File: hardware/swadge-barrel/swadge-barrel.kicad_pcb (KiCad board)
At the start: 2 copper layers, 70.4 x 89.6 mm, 48 parts, among them J1 USB_B_Micro, Q1 Q_NPN_BEC, SW1 SW_SPDT, U1 ESP-13-WROOM-02D, U2 OLED_DISPLAY, U3 BUS_PCIexpress, U4 QMA6981, U5 AP1117-33, U6 OLED_CONNECTOR

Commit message: Fixed 3D model paths, Updated to version 1.0.1
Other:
- board text added: "Barrel 1.0.1"
- board text removed: "Barrel 1.0.0"

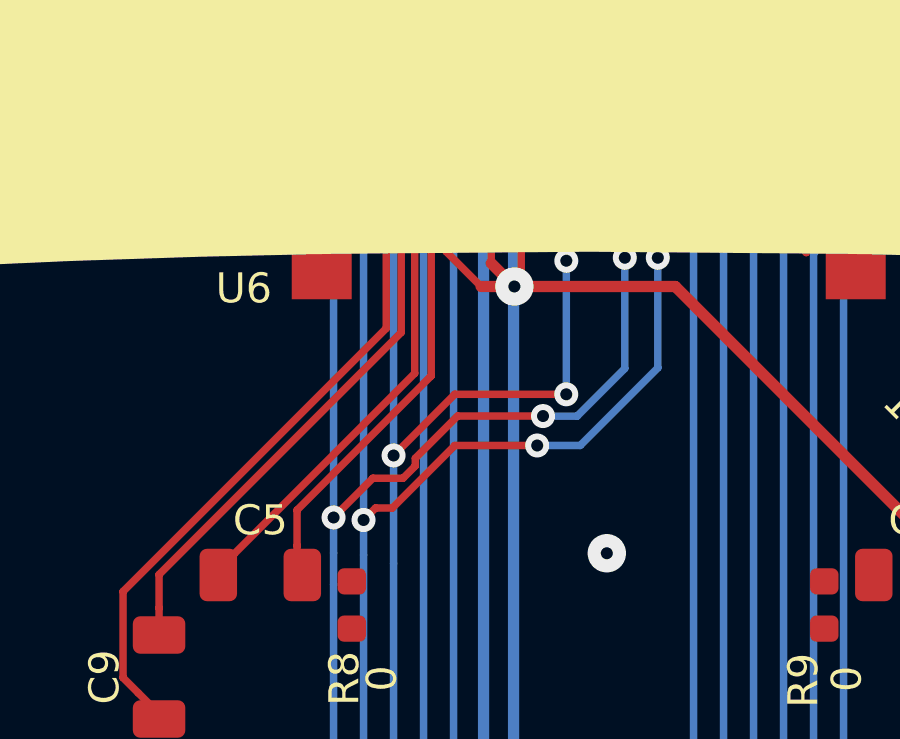
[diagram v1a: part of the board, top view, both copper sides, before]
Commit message: Fixed some bent traces
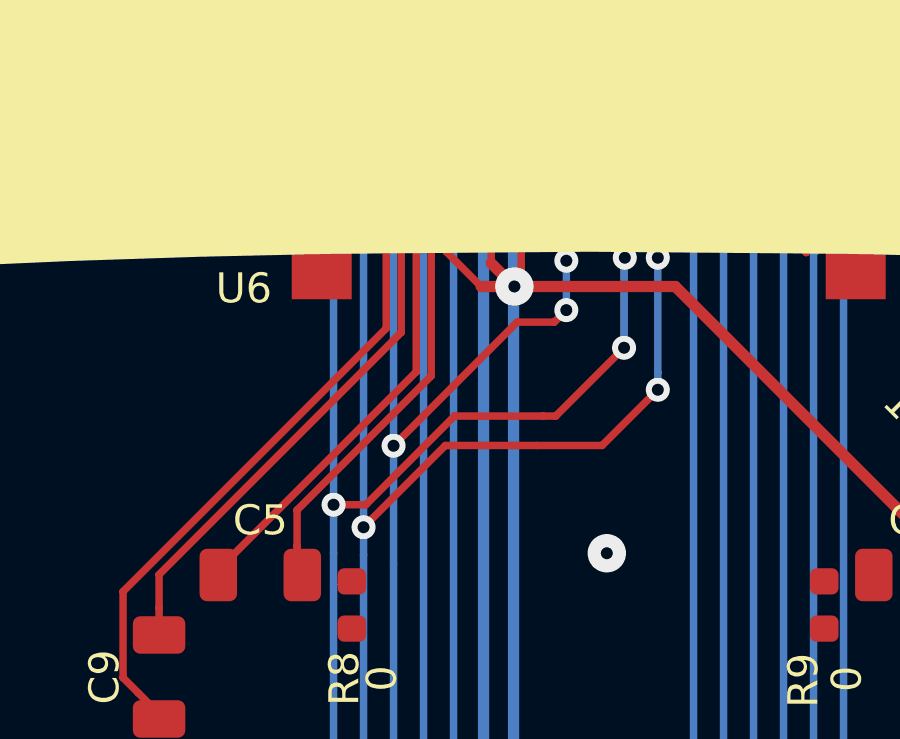
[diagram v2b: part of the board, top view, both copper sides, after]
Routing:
- net _RES: track 126.7 -> 124.9 mm
- net SCL: track 139.9 -> 139.2 mm
- net SDA: track 145.9 -> 146.4 mm

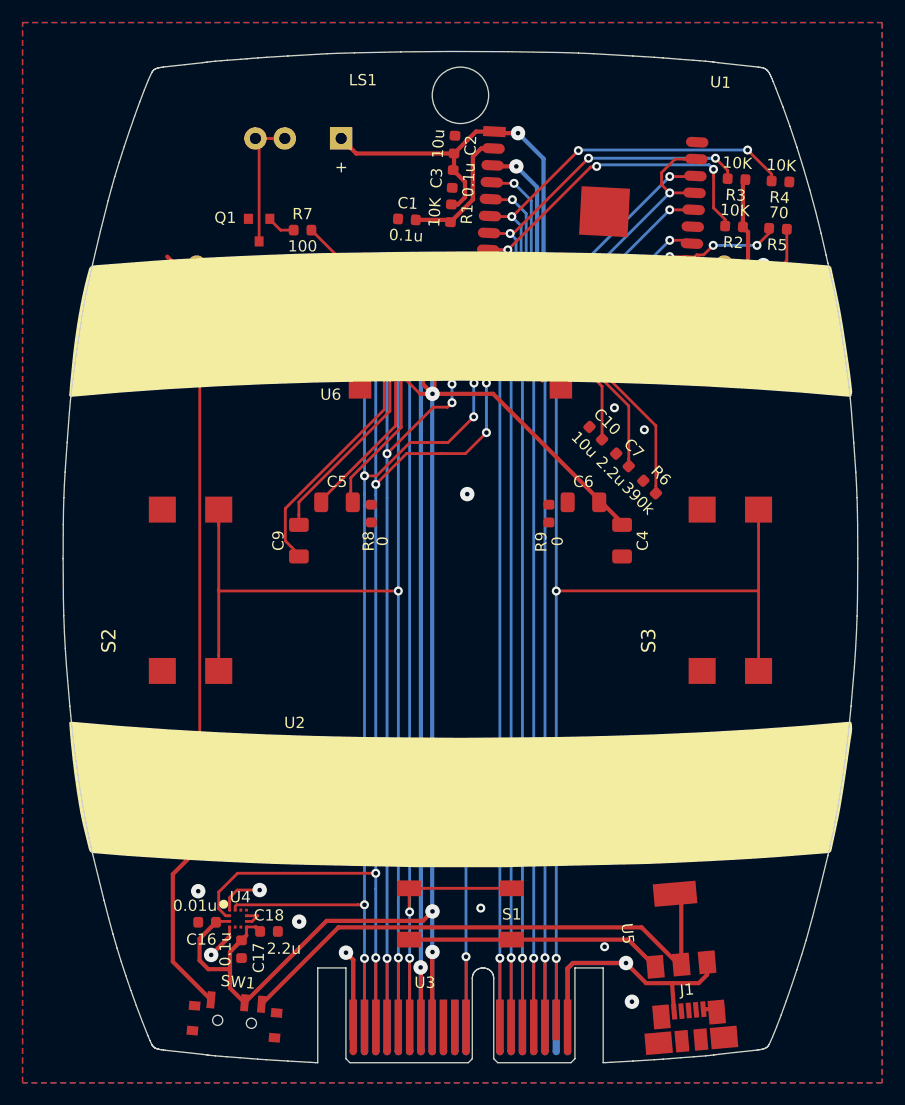
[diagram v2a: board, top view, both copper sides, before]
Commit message: #26 Remapped buttons to match devkit gpios
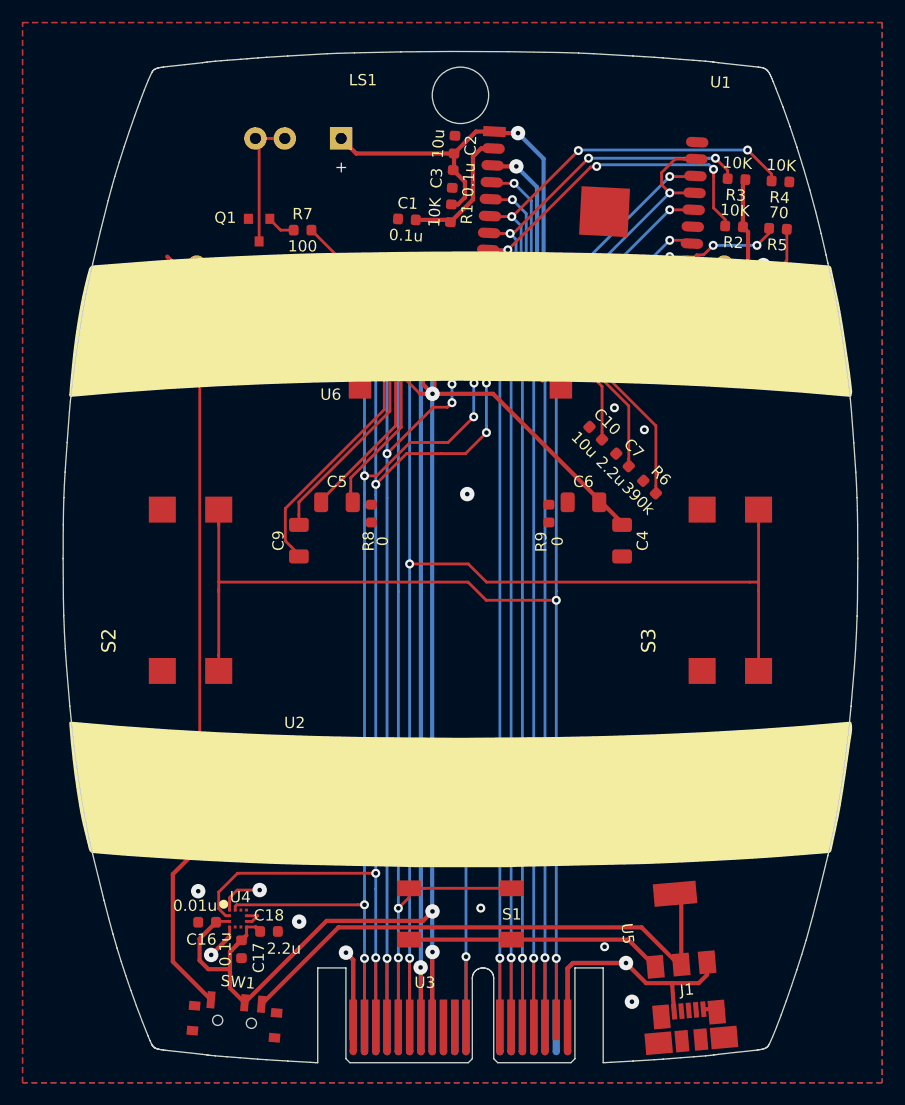
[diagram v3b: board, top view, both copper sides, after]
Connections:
- J1 pad 2: (no net) -> Net-(J1-Pad2)
- J1 pad 3: (no net) -> Net-(J1-Pad3)
- J1 pad 4: (no net) -> Net-(J1-Pad4)
- S1 pad 1: SW1 -> SW2
- S1 pad 2: SW1 -> SW2
- S2 pad 1: SW2 -> SW3
- S2 pad 2: SW2 -> SW3
- S3 pad 1: SW3 -> SW1
- S3 pad 2: SW3 -> SW1
- U4 pad 10: (no net) -> Net-(U4-Pad10)
- U4 pad 11: (no net) -> Net-(U4-Pad11)
- U4 pad 5: (no net) -> Net-(U4-Pad5)
- U4 pad 6: (no net) -> Net-(U4-Pad6)
- U6 pad 7: (no net) -> Net-(U6-Pad7)
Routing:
- net SW1: track 100.1 -> 134.7 mm
- net SW2: track 119.1 -> 98.7 mm
- net SW3: track 110.5 -> 124.7 mm

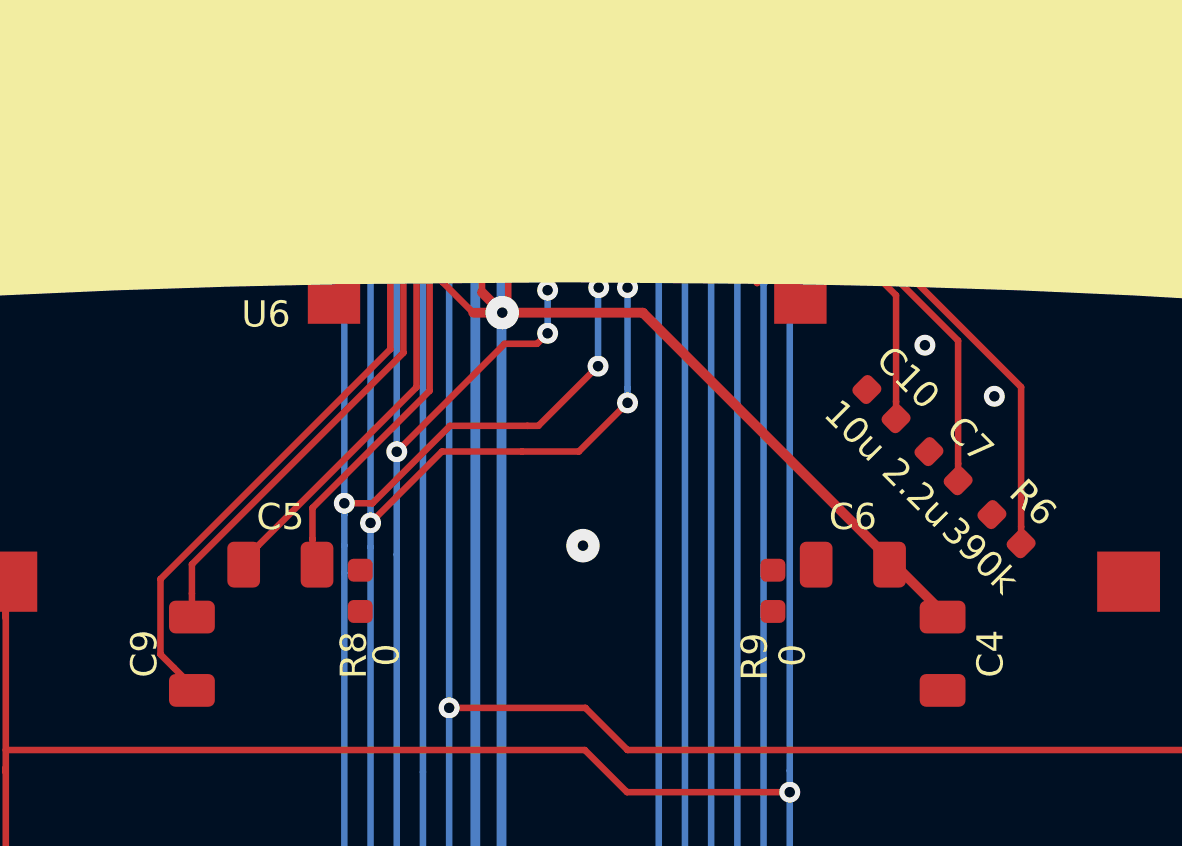
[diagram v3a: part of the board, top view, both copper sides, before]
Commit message: Flipped OLED contacts, haven't routed them yet #24
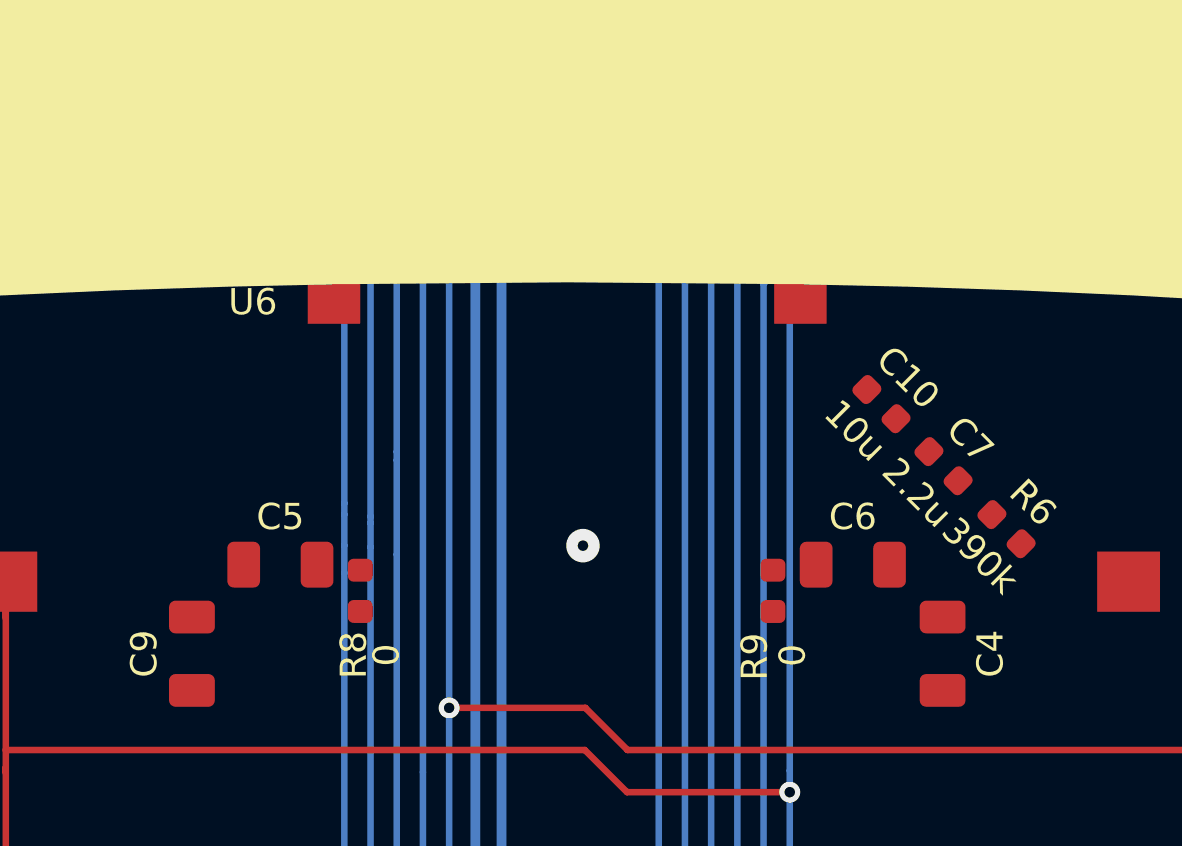
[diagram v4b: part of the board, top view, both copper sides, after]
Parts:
- U6: footprint Swadge_Parts:oled-flat_copy -> Swadge_Parts:ER-OLED0.96-1.3
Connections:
- U6 pad 31: (no net) -> GND
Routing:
- net GND: track 90.1 -> 54.7 mm, vias 13 -> 11
- net +3V3: track 305.2 -> 271.3 mm, vias 6 -> 5
- net Net-(R6-Pad2): track 23.3 -> 0.00 mm
- net Net-(C9-Pad1): track 21.8 -> 0.00 mm
- net SDA: track 146.4 -> 125.1 mm, vias 8 -> 5
- net Net-(C7-Pad2): track 18.6 -> 0.00 mm
- net Net-(C9-Pad2): track 18.2 -> 0.00 mm
- net SCL: track 139.2 -> 121.8 mm, vias 8 -> 5
- net Net-(C5-Pad1): track 15.8 -> 0.00 mm
- net Net-(C5-Pad2): track 14.9 -> 0.00 mm
- net Net-(C10-Pad2): track 13.9 -> 0.00 mm
- net _RES: track 124.9 -> 113.0 mm, vias 7 -> 4

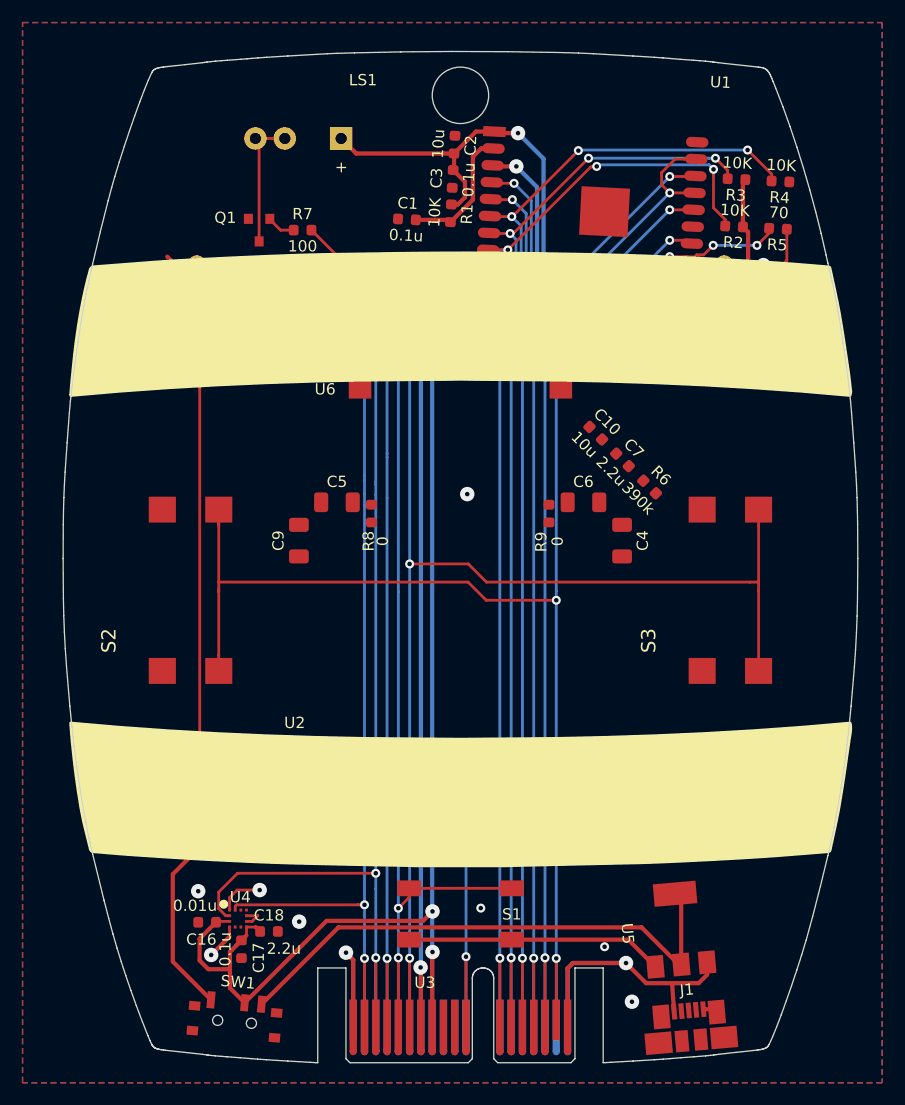
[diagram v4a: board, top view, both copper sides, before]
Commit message: #24 Rerouted OLED traces
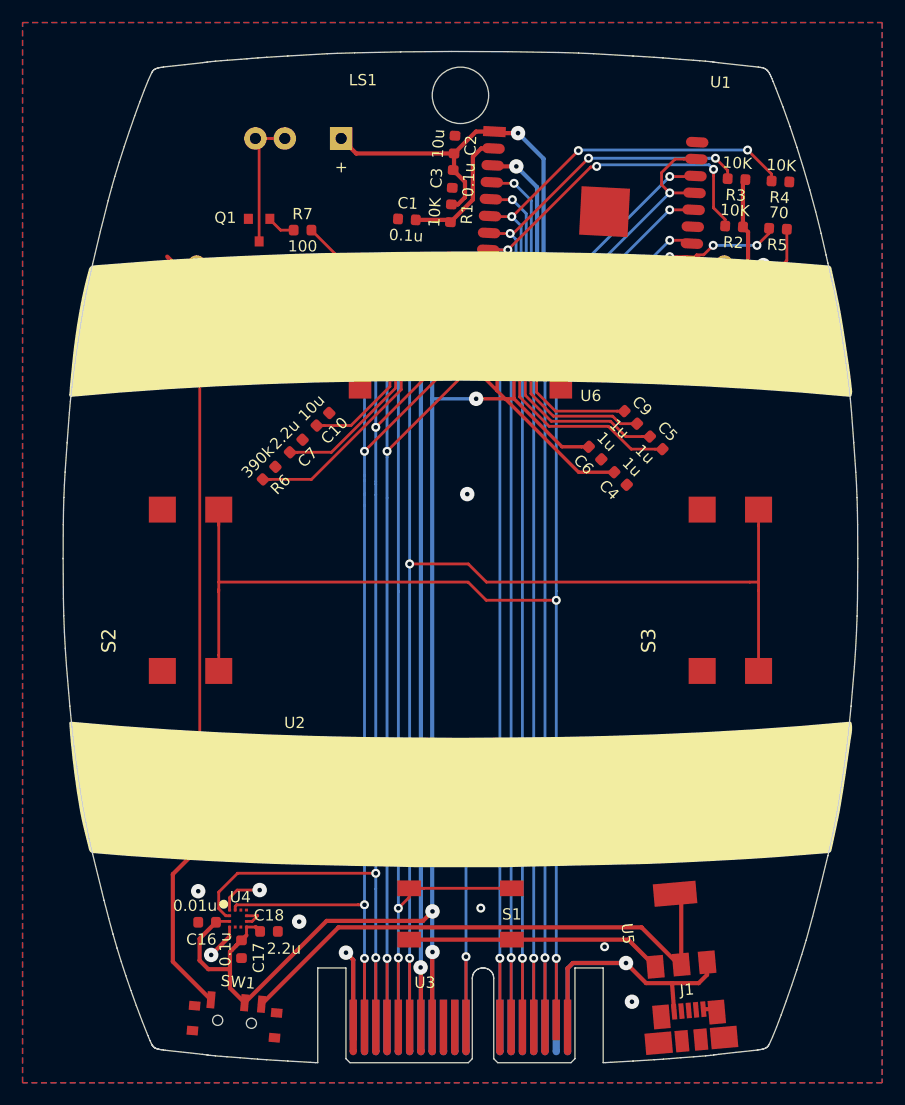
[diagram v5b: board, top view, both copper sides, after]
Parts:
- removed R8, R9: 0, Swadge_Parts:R_0603_1608Metric
- C4, C5, C6, C9: footprint Swadge_Parts:C_1206_3216Metric -> Swadge_Parts:C_0603_1608Metric
- moved R6 33.7 mm to (128.5, 90.7), turned to 225 degrees
- moved C9 31.4 mm to (160.6, 85.8), turned to 315 degrees
- moved C7 28.9 mm to (130.9, 88.3), turned to 225 degrees
- moved C5 28.8 mm to (162.8, 88.1), turned to 315 degrees
- moved C10 24.2 mm to (133.3, 86.0), turned to 225 degrees
- moved C4 5.51 mm to (159.7, 91.2), turned to 135 degrees
- moved C6 4.48 mm to (157.4, 89.0), turned to 135 degrees
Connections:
- J1 pad 2: Net-(J1-Pad2) -> (no net)
- J1 pad 3: Net-(J1-Pad3) -> (no net)
- J1 pad 4: Net-(J1-Pad4) -> (no net)
- U4 pad 10: Net-(U4-Pad10) -> (no net)
- U4 pad 11: Net-(U4-Pad11) -> (no net)
- U4 pad 5: Net-(U4-Pad5) -> (no net)
- U4 pad 6: Net-(U4-Pad6) -> (no net)
- U6 pad 7: Net-(U6-Pad7) -> (no net)
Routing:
- net +3V3: track 271.3 -> 310.9 mm, vias 5 -> 6
- net GND: track 54.7 -> 88.8 mm
- net Net-(R6-Pad2): track 0.00 -> 18.6 mm
- net Net-(C5-Pad2): track 0.00 -> 18.3 mm
- net Net-(C5-Pad1): track 0.00 -> 16.1 mm
- net Net-(C7-Pad2): track 0.00 -> 14.6 mm
- net Net-(C9-Pad2): track 0.00 -> 13.9 mm
- net Net-(C9-Pad1): track 0.00 -> 11.8 mm
- net _RES: track 113.0 -> 124.6 mm, vias 4 -> 5
- net SCL: track 121.8 -> 133.3 mm, vias 5 -> 6
- net Net-(C10-Pad2): track 0.00 -> 10.7 mm
- net SDA: track 125.1 -> 135.2 mm, vias 5 -> 6

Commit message: Organized passives
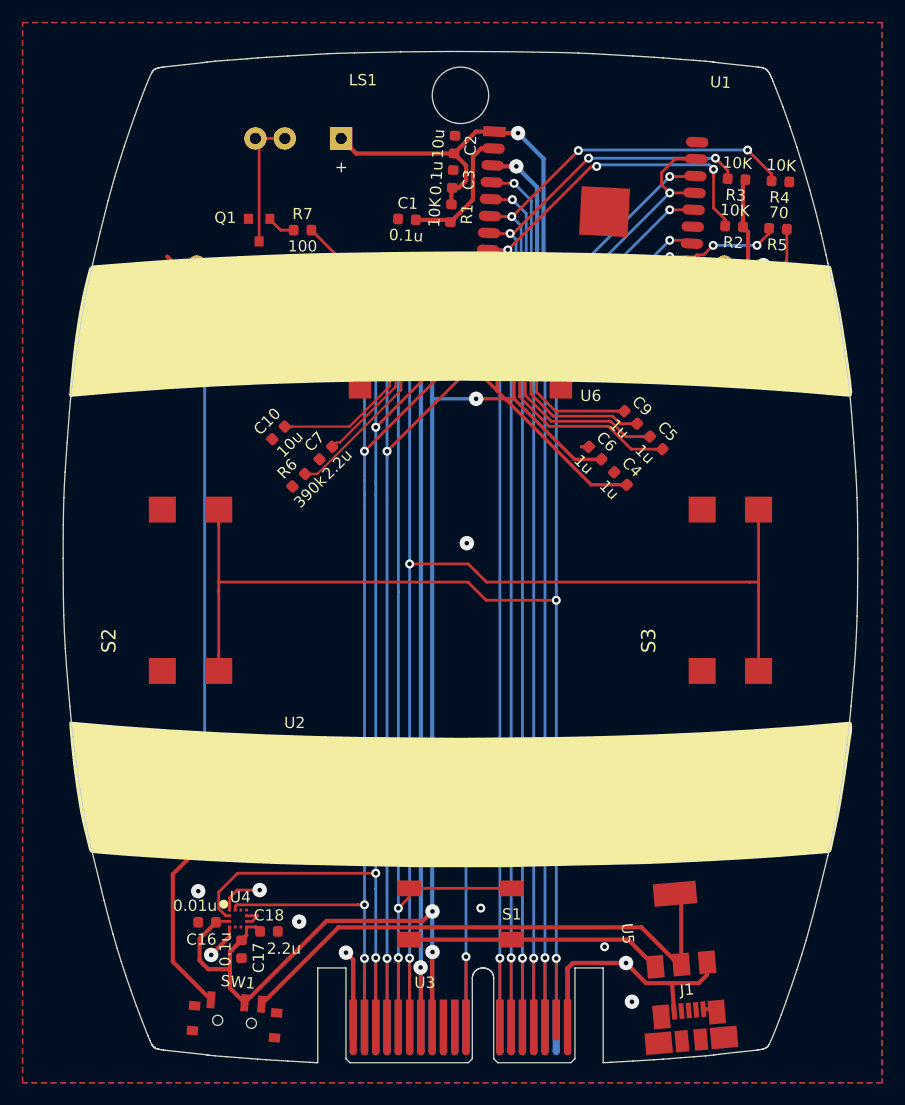
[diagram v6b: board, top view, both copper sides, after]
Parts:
- moved C10 4.12 mm to (129.4, 87.2), turned to 45 degrees
- moved C7 2.70 mm to (133.6, 89.0), turned to 45 degrees
- moved R6 2.70 mm to (131.2, 91.4), turned to 45 degrees
- turned C3 to 267 degrees
- turned C4 to 315 degrees
- turned C6 to 315 degrees
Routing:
- net Net-(C7-Pad2): track 14.6 -> 10.6 mm
- net Net-(R6-Pad2): track 18.6 -> 14.7 mm
- net +3V3: track 310.9 -> 314.1 mm
- net Net-(C10-Pad2): track 10.7 -> 13.5 mm
- net Net-(D3-Pad2): track 41.8 -> 43.6 mm, vias 0 -> 2
- net GND: track 88.8 -> 89.4 mm
